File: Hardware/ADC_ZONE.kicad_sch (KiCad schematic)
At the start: 9 parts

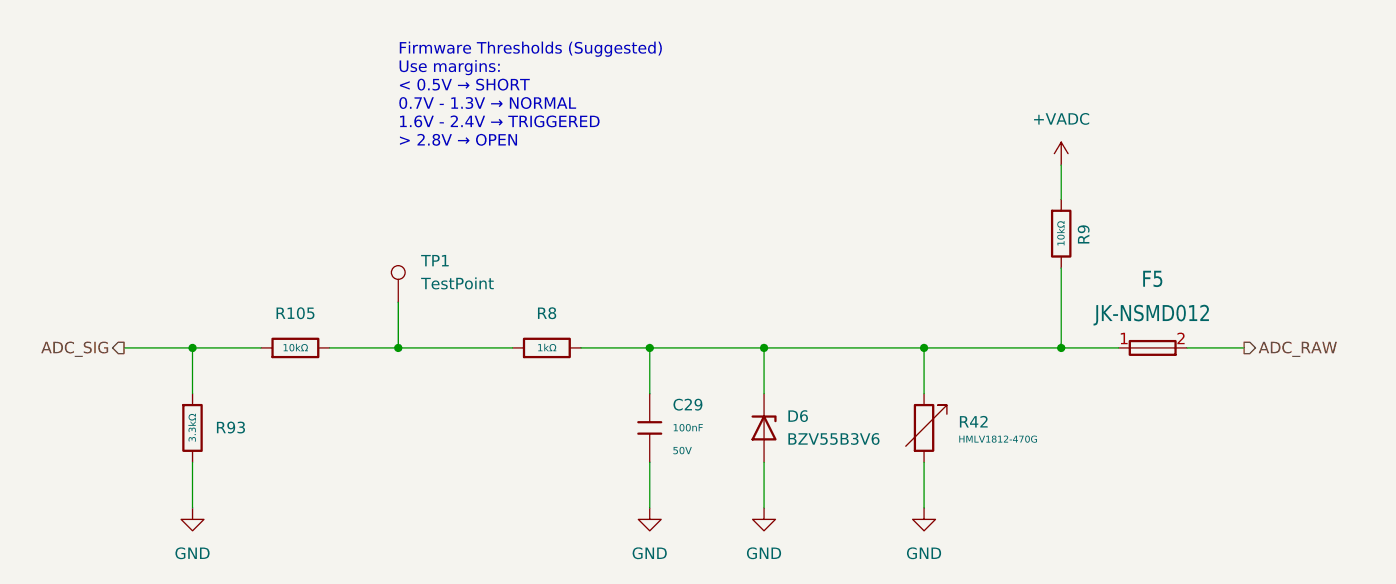
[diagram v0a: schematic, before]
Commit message: remove unused sheets
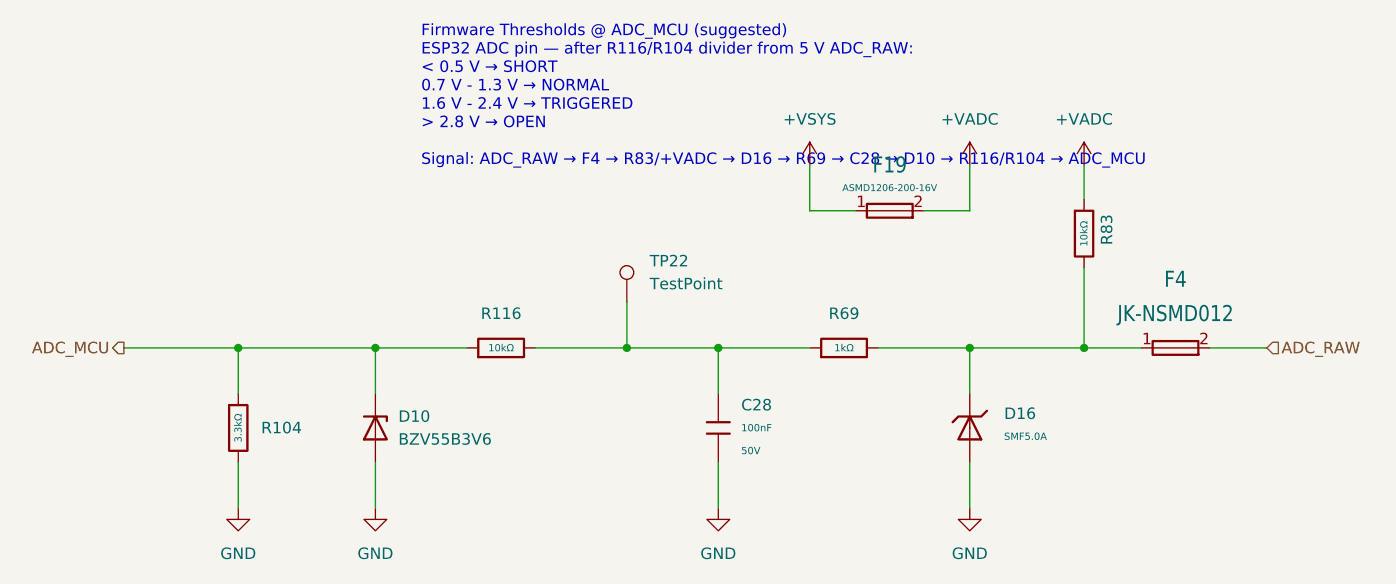
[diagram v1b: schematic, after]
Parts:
- removed D6: BZV55B3V6, Diode_SMD:D_MiniMELF, symbol Diode:BZV55B3V6
- removed R42: HMLV1812-470G, Resistor_SMD:R_1812_4532Metric_Pad1.30x3.40mm_HandSolder, symbol PCM_JLCPCB-Extended:MOV, HMLV1812-470G
- added D10: BZV55B3V6, Diode_SMD:D_MiniMELF, symbol Diode:BZV55B3V6
- added D16: SMF5.0A, PCM_JLCPCB:D_SOD-123FL, symbol PCM_JLCPCB-Diodes:TVS-Uni,SMF5.0A
- added F19: ASMD1206-200-16V, EASYEDA2KICAD:F1206, symbol PCM_JLCPCB-Extended:Fuse, ASMD1206-200-16V
- F4: renamed from F5; footprint EasyEDA:F1206 -> EASYEDA2KICAD:F1206
- renumbered C29 to C28, R93 to R104, R105 to R116, R8 to R69, R9 to R83, TP1 to TP22
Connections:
- net +VADC: now also F19.2
- net GND: now also D10.2 (A), D16.2
- net at F4.1, R69.2, R83.2: now also D16.1; no longer C28.1
- net at R116.2, R69.1, TP22.1: now also C28.1
- net ADC_SIG renamed ADC_MCU
- net ADC_MCU: now also D10.1 (K)
- new net +VSYS: F19.1
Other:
- note added: "Firmware Thresholds @ ADC_MCU (suggested) ESP32 ADC pin — after R116/R104 divider from 5 V ADC_RAW: < 0.5 V → SHORT 0.7 V - 1.3 V → NORMAL 1.6 V - 2.4 V → TRIGGERED > 2.8 V → OPEN Signal: ADC_RAW → F4 → R83/+VADC → D16 → R69 → C28 → D10 → R116/R104 → ADC_MCU"
- note removed: "Firmware Thresholds (Suggested) Use margins: < 0.5V → SHORT 0.7V - 1.3V → NORMAL 1.6V - 2.4V → TRIGGERED > 2.8V → OPEN"
- moved on the sheet: C28, F4, R104, R116, R69, R83, TP22
